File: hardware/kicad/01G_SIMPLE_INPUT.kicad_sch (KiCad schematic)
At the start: 5 parts, among them J901 BAT_ACC_GND_PIGTAIL

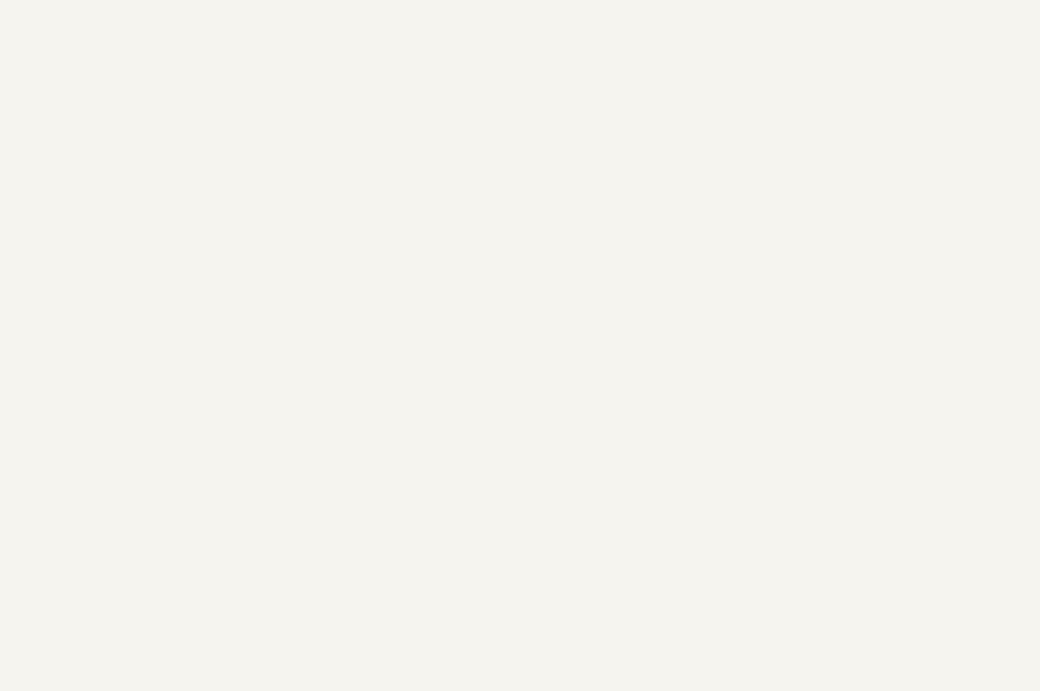
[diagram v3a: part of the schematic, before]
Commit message: fix(power): represent existing vehicle source and export external fuse candidates
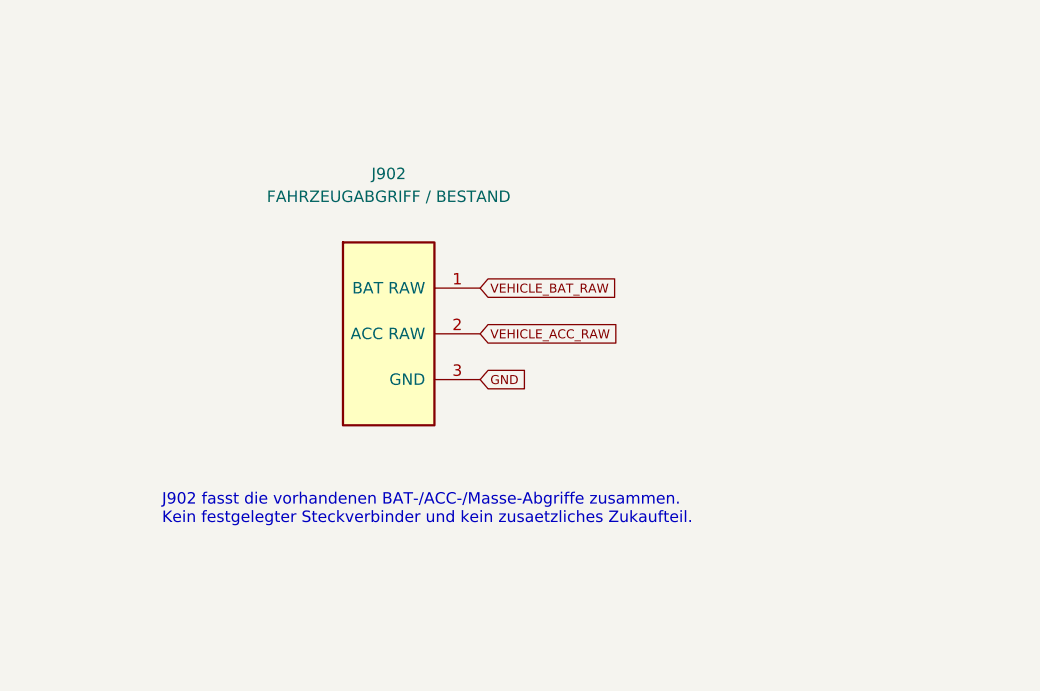
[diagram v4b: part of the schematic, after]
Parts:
- added J902: FAHRZEUGABGRIFF / BESTAND, symbol TripTracer_V1:VEHICLE_SOURCE_3WIRE
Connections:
- net GND: now also J902.3 (GND)
- net VEHICLE_ACC_RAW: now also J902.2 (ACC RAW)
- net VEHICLE_BAT_RAW: now also J902.1 (BAT RAW)
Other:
- note added: "J902 fasst die vorhandenen BAT-/ACC-/Masse-Abgriffe zusammen. Kein festgelegter Steckverbinder und kein zusaetzliches Zukaufteil."
